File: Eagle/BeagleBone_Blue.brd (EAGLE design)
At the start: 86.4 x 54.6 mm, 281 parts, among them M1 JST_ZH_2, M2 JST_ZH_2, M3 JST_ZH_2, M4 JST_ZH_2, P10 SCHA5B0200, Q3 MOSFET-N, U1 TPD4S012_DRY_6, U4 TPD4S012_DRY_6, U5 24LC_32AT-I/OT, U6 SN74LVC1G07_DCK_5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

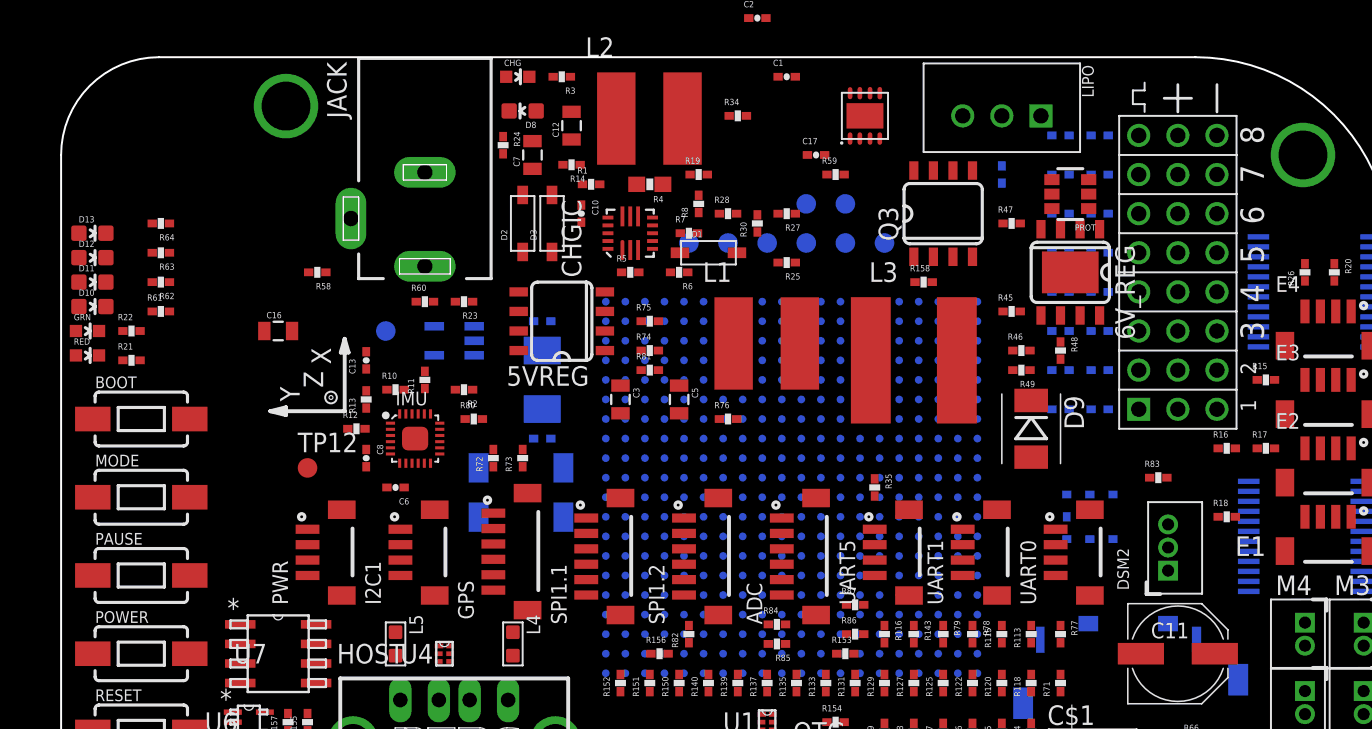
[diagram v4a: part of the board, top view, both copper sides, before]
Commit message: change DSM2 connector to surface mount & move buttons
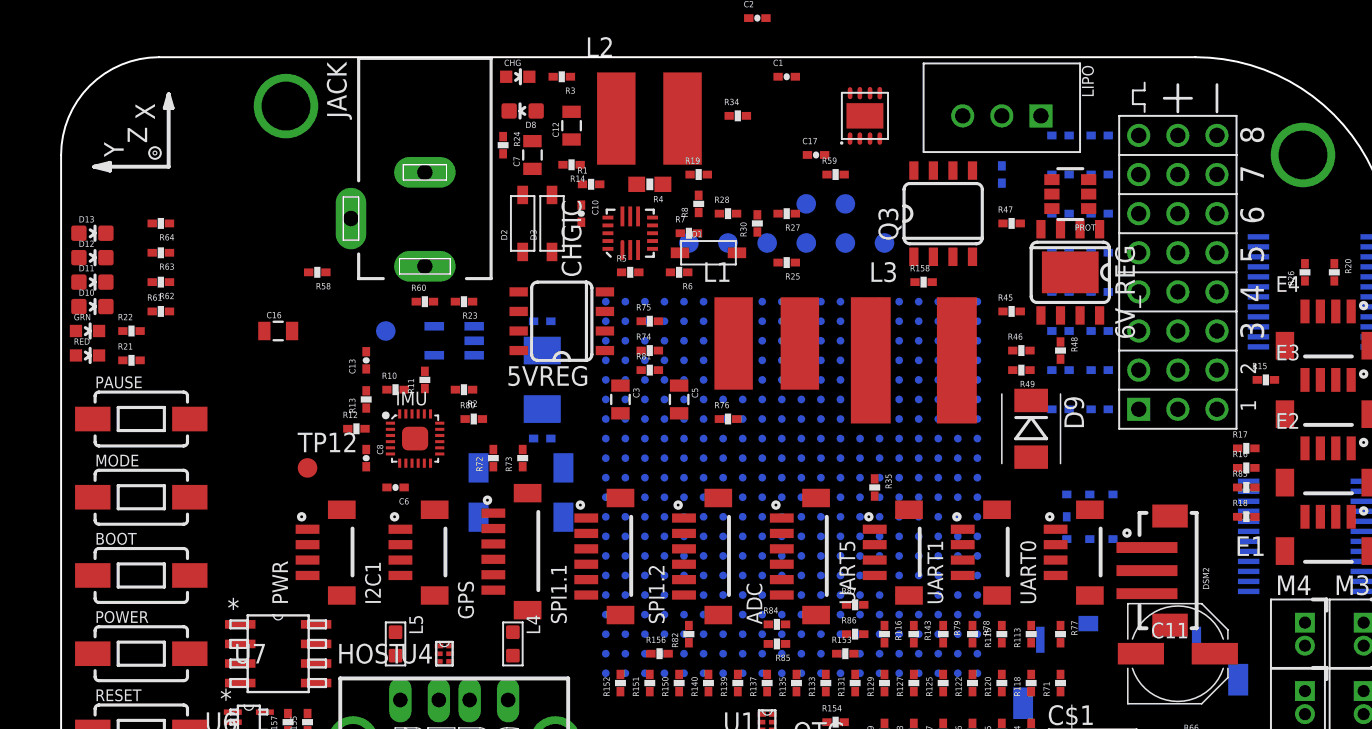
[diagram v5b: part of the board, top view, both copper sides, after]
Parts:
- DSM2: value JST_ZH_3 -> JST_ZH_3SMD_TOP; device Strawson_Eagle_Lib:JST_ZH_3 -> Strawson_Eagle_Lib:JST_ZH_3_SMD_TOP
- moved U$5 19.6 mm to (6.86, -7.11)
- moved BOOT 10.2 mm to (5.08, -33.7)
- moved PAUSE 10.2 mm to (5.08, -23.5)
- moved R83 5.75 mm to (76.8, -27.9)
- moved R16 1.80 mm to (76.8, -26.7)
- moved R17 1.27 mm to (76.8, -25.4)
- moved R18 1.27 mm to (76.8, -29.8)
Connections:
- net 3.3V: now also DSM2.1; no longer DSM2.P$1
- net GND: now also DSM2.2; no longer DSM2.P$2
- net UART4_RX: now also DSM2.3; no longer DSM2.P$3

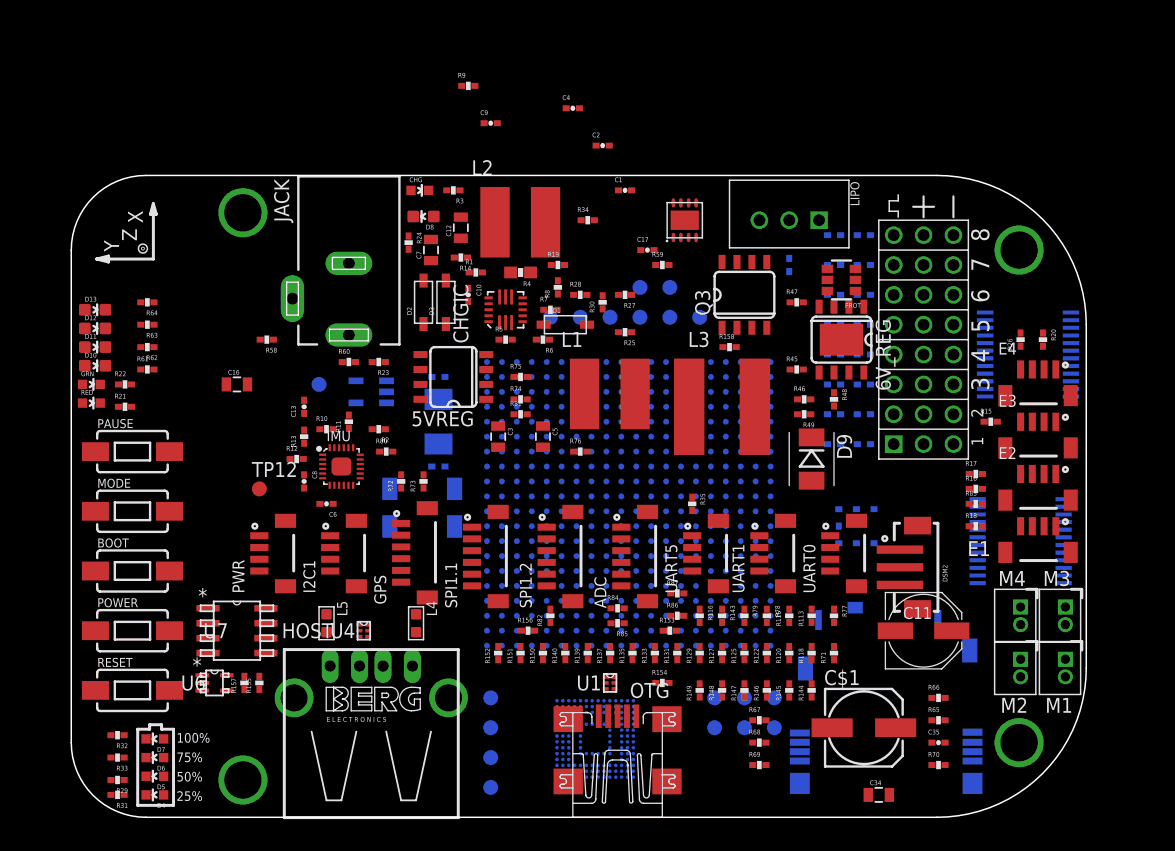
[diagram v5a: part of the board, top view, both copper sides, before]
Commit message: shuffle motor & encoder connectors
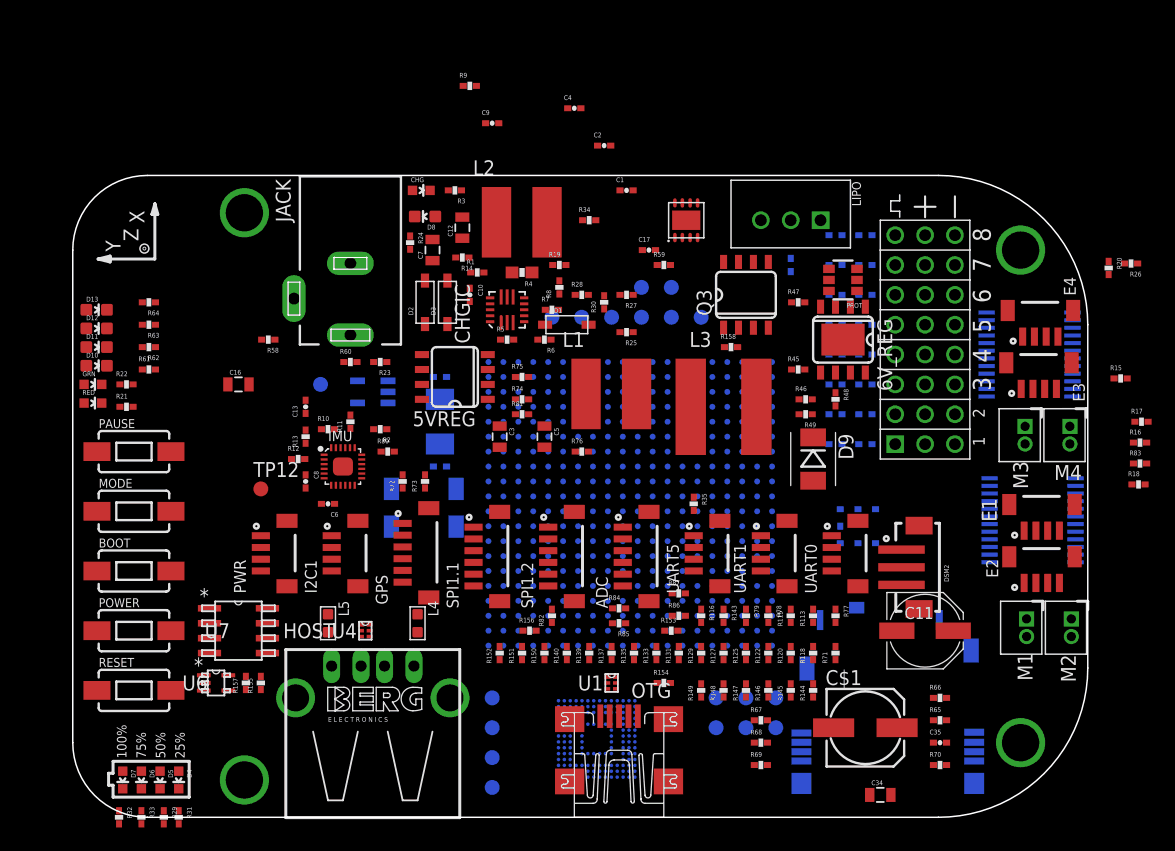
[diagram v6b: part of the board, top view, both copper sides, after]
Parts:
- moved M4 15.9 mm to (84.8, -22.1)
- moved M3 15.7 mm to (81.0, -22.1)
- moved R17 14.8 mm to (90.9, -21.0)
- moved R16 14.5 mm to (90.8, -22.7)
- moved R83 14.4 mm to (90.8, -24.5)
- moved R18 14.3 mm to (90.7, -26.3)
- moved R15 11.6 mm to (89.2, -17.3)
- moved R26 11.4 mm to (90.0, -7.49), turned to 180 degrees
- moved R20 8.27 mm to (88.1, -7.87)
- moved R32 6.99 mm to (3.94, -54.6), turned to 270 degrees
- moved E3 5.71 mm to (81.2, -16.9), turned to 180 degrees
- moved E4 5.66 mm to (81.3, -12.4), turned to 180 degrees
- moved R31 5.54 mm to (9.02, -54.6), turned to 270 degrees
- moved M2 5.51 mm to (85.0, -38.5)
- moved R33 5.47 mm to (5.84, -54.6), turned to 270 degrees
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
